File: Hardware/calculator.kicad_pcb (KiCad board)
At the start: 2 copper layers, 70.7 x 143.2 mm, 49 parts, among them J1 Sharp_LCD_10Pin

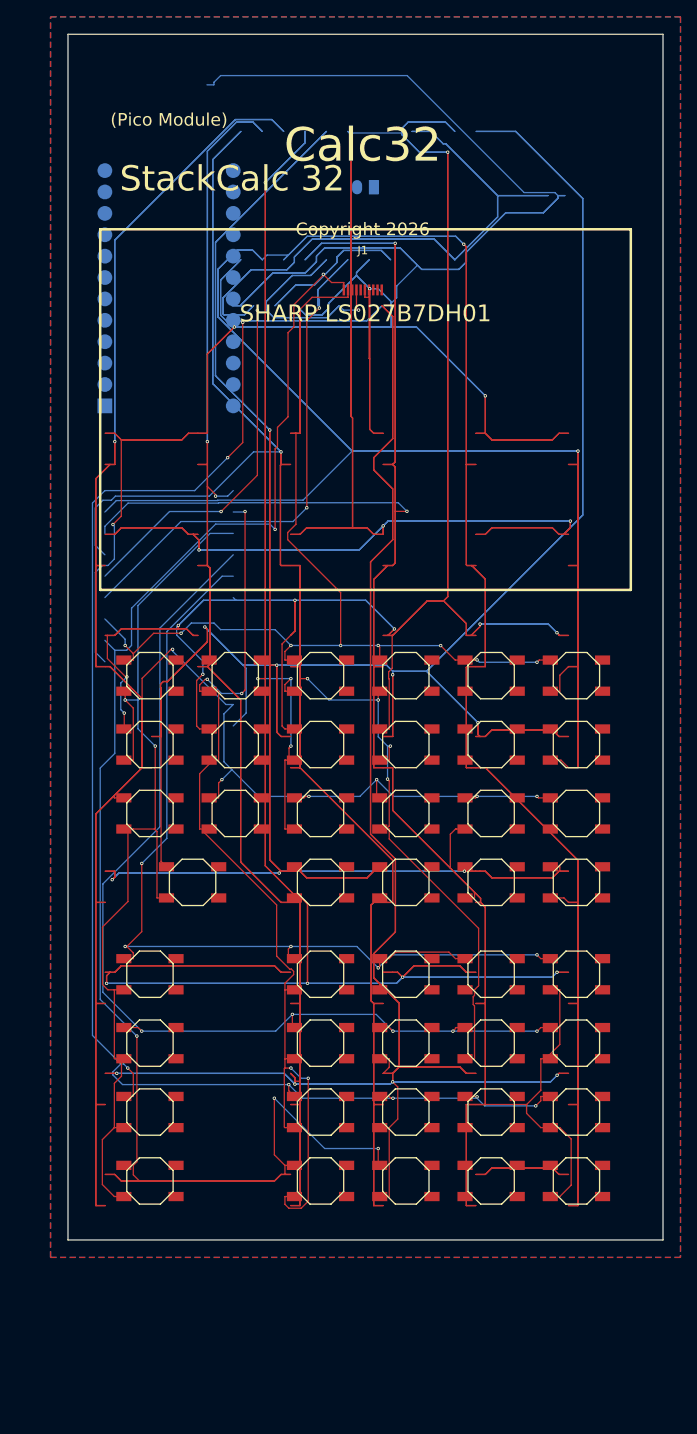
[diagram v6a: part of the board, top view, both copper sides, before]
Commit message: refactor: reorganize hardware manufacturing files, remove legacy build outputs, and update project structure for firmware and UI components.
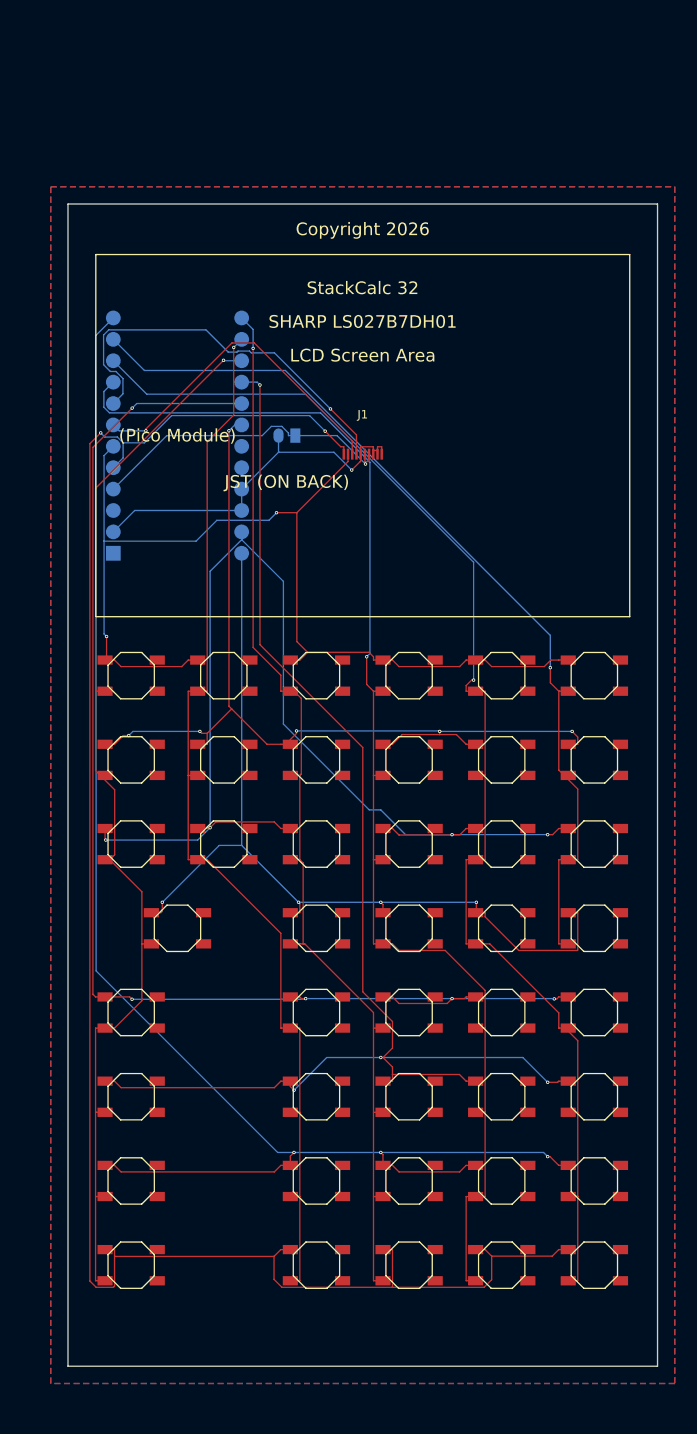
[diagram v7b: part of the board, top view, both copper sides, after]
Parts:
- moved JST1 30.9 mm to (36.0, -110.5)
- moved J1 19.5 mm to (45.0, -110.5)
- moved MCU1 17.5 mm to (23.0, -110.5)
- moved B21 10.2 mm to (17.5, -12.0)
- moved B37 10.2 mm to (72.5, -12.0)
- moved B33 10.1 mm to (61.5, -12.0)
- moved B25 10.0 mm to (39.5, -12.0)
- moved B29 10.0 mm to (50.5, -12.0)
- moved B20 8.48 mm to (17.5, -22.0)
- moved B36 8.45 mm to (72.5, -22.0)
- moved B32 8.28 mm to (61.5, -22.0)
- moved B24 8.20 mm to (39.5, -22.0)
- moved B28 8.19 mm to (50.5, -22.0)
- moved B19 6.74 mm to (17.5, -32.0)
- moved B35 6.71 mm to (72.5, -32.0)
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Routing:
- net P9: track 1076.5 -> 130.3 mm, vias 14 -> 1
- net P1: track 694.3 -> 105.0 mm, vias 8 -> 4
- net P4: track 608.4 -> 113.2 mm, vias 13 -> 6
- net P16: track 560.2 -> 109.4 mm, vias 2 -> 1
- net VCC: track 419.6 -> 37.6 mm, vias 4 -> 1
- net P0: track 389.8 -> 137.9 mm, vias 7 -> 4
- net P15: track 394.4 -> 154.5 mm, vias 5 -> 1
- net P14: track 370.0 -> 155.5 mm, vias 2 -> 1
- net GND: track 134.1 -> 44.9 mm, vias 0 -> 1
- net P21: track 264.6 -> 217.1 mm, vias 5 -> 2
- net P10: track 225.5 -> 181.6 mm, vias 7 -> 3
- net P18: track 89.0 -> 47.8 mm, vias 3 -> 1
- net P6: track 122.6 -> 163.4 mm, vias 5 -> 4
- net P5: track 119.7 -> 155.1 mm
- net P19: track 67.9 -> 39.5 mm, vias 2 -> 1
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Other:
- board size 70.7 x 143.2 mm -> 70 x 138 mm
- board text added: "JST (ON BACK)"
- board text added: "LCD Screen Area"
- board text removed: "Calc32"

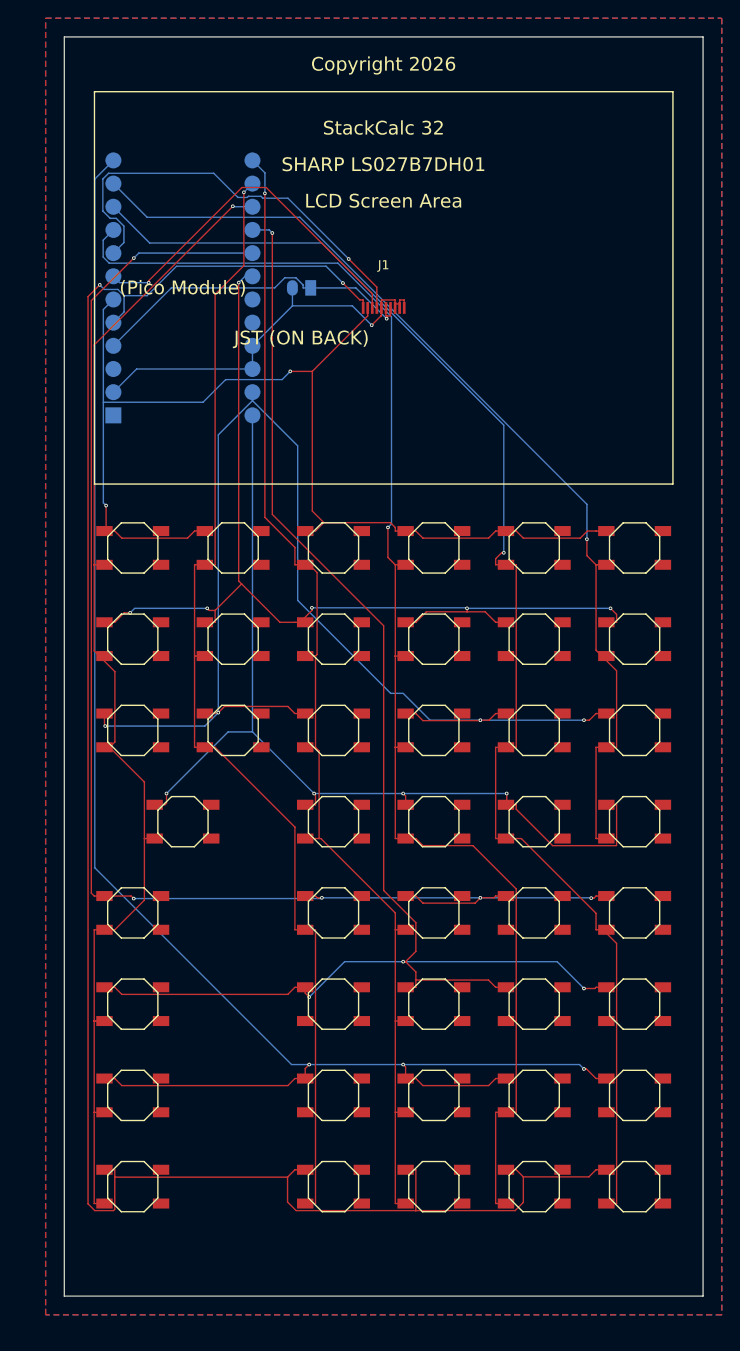
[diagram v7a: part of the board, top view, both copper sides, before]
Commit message: refactor: transition UI rendering to direct canvas primitives and update Firmware UART input handling
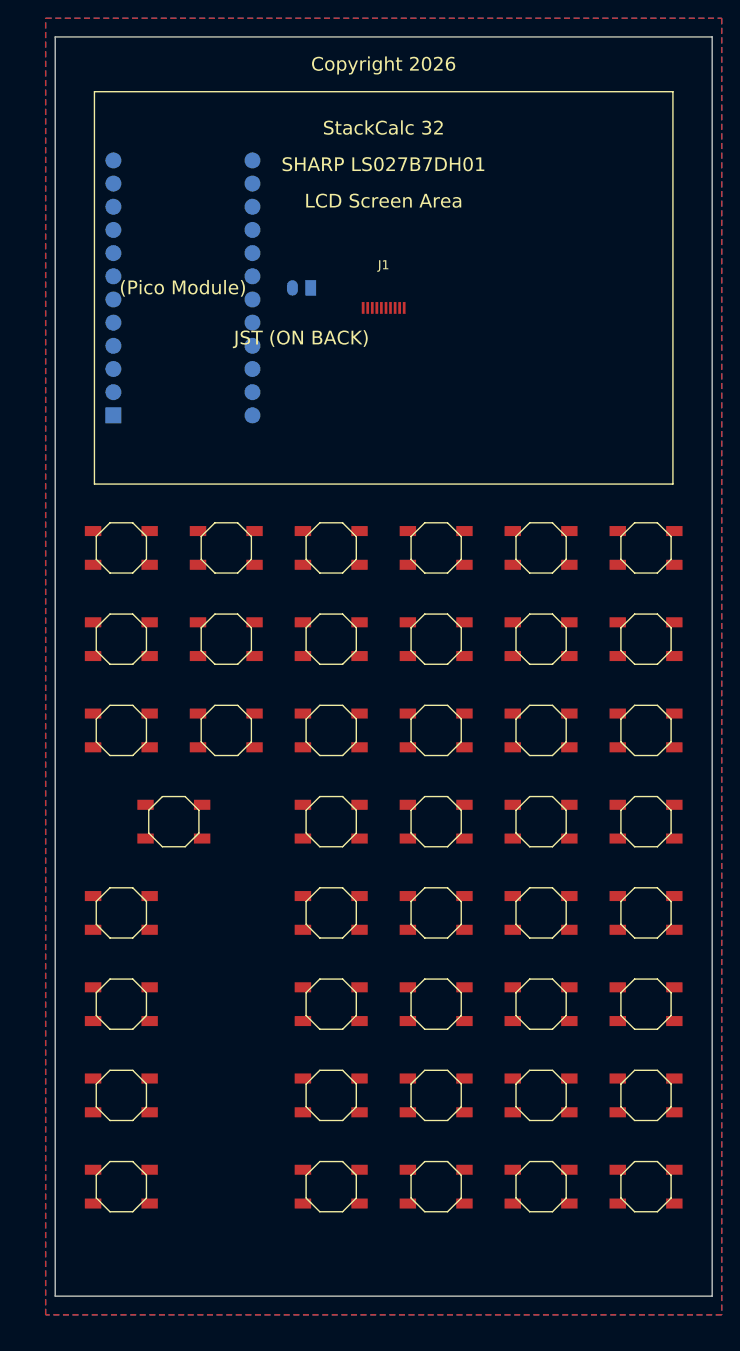
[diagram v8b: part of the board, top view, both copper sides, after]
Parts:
- moved B15 1.25 mm to (73.8, -52.0)
- moved B16 1.25 mm to (73.8, -62.0)
- moved B17 1.25 mm to (73.8, -72.0)
- moved B18 1.25 mm to (16.2, -42.0)
- moved B19 1.25 mm to (16.2, -32.0)
- moved B2 1.25 mm to (16.2, -62.0)
- moved B20 1.25 mm to (16.2, -22.0)
- moved B21 1.25 mm to (16.2, -12.0)
- moved B3 1.25 mm to (16.2, -72.0)
- moved B34 1.25 mm to (73.8, -42.0)
- moved B35 1.25 mm to (73.8, -32.0)
- moved B36 1.25 mm to (73.8, -22.0)
- moved B37 1.25 mm to (73.8, -12.0)
- moved SOFT1 1.25 mm to (16.2, -82.0)
- moved SOFT6 1.25 mm to (73.8, -82.0)
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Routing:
- net P21: track 217.1 -> 0.00 mm, vias 2 -> 0
- net P10: track 181.6 -> 0.00 mm, vias 3 -> 0
- net P6: track 163.4 -> 0.00 mm, vias 4 -> 0
- net P14: track 155.5 -> 0.00 mm, vias 1 -> 0
- net P5: track 155.1 -> 0.00 mm, vias 5 -> 0
- net P15: track 154.5 -> 0.00 mm, vias 1 -> 0
- net P0: track 137.9 -> 0.00 mm, vias 4 -> 0
- net P7: track 130.9 -> 0.00 mm, vias 1 -> 0
- net P9: track 130.3 -> 0.00 mm, vias 1 -> 0
- net P8: track 128.4 -> 0.00 mm, vias 1 -> 0
- net P20: track 123.8 -> 0.00 mm, vias 2 -> 0
- net P4: track 113.2 -> 0.00 mm, vias 6 -> 0
- net P16: track 109.4 -> 0.00 mm, vias 1 -> 0
- net P1: track 105.0 -> 0.00 mm, vias 4 -> 0
- net P18: track 47.8 -> 0.00 mm, vias 1 -> 0
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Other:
- board size 70 x 138 mm -> 72 x 138 mm
